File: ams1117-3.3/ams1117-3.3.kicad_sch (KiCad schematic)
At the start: 0 parts

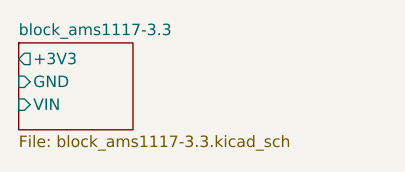
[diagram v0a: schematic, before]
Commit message: finalised AMS1117
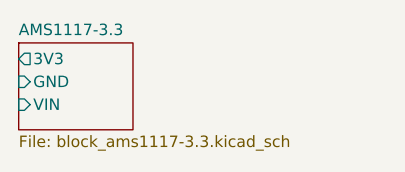
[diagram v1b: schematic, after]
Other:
- sheet block_ams1117-3.3 renamed AMS1117-3.3
- sheet AMS1117-3.3 ports: added 3V3; removed +3V3
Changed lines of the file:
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@@
 			(color 0 0 0 0.0000)
 		)
-		(property "Sheetname" "block_ams1117-3.3"
+		(property "Sheetname" "AMS1117-3.3"
 			(at 60.96 41.9604 0)
 			(effects
@@
 			)
 		)
-		(pin "+3V3" output
+		(pin "3V3" output
 			(at 60.96 44.45 180)
 			(effects
